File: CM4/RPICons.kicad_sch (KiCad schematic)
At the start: 2 parts, among them U1 Compute_Module_4_Connectors, U2 Compute_Module_4_Connectors

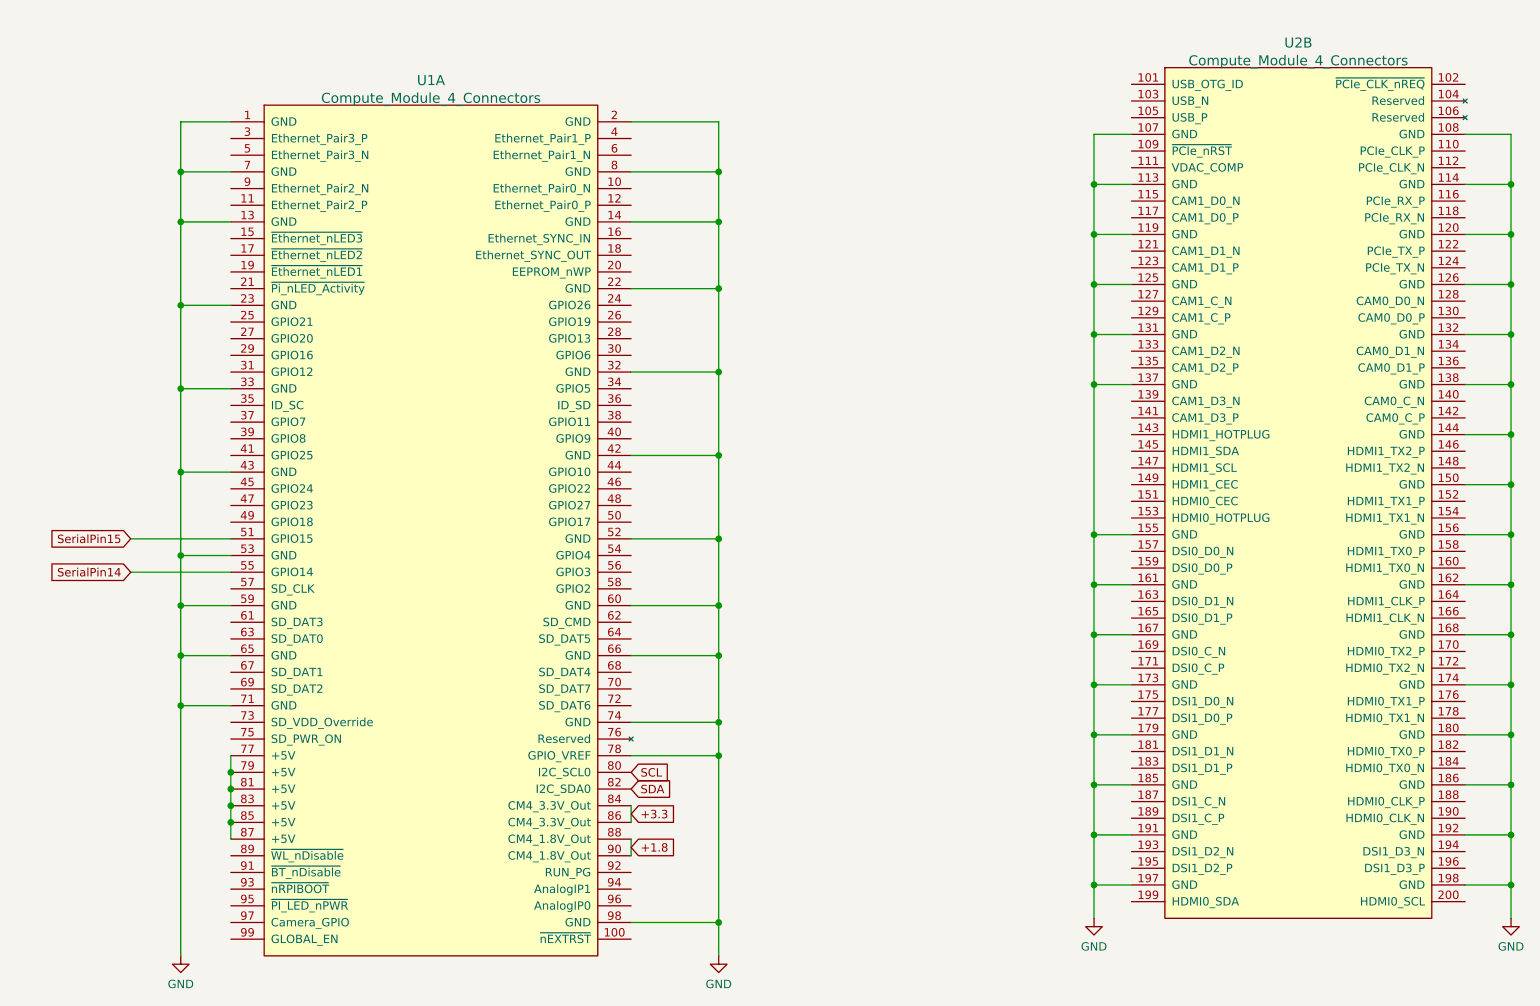
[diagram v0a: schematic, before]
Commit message: Added Power Control Relay
also cleaned up some junk and jank
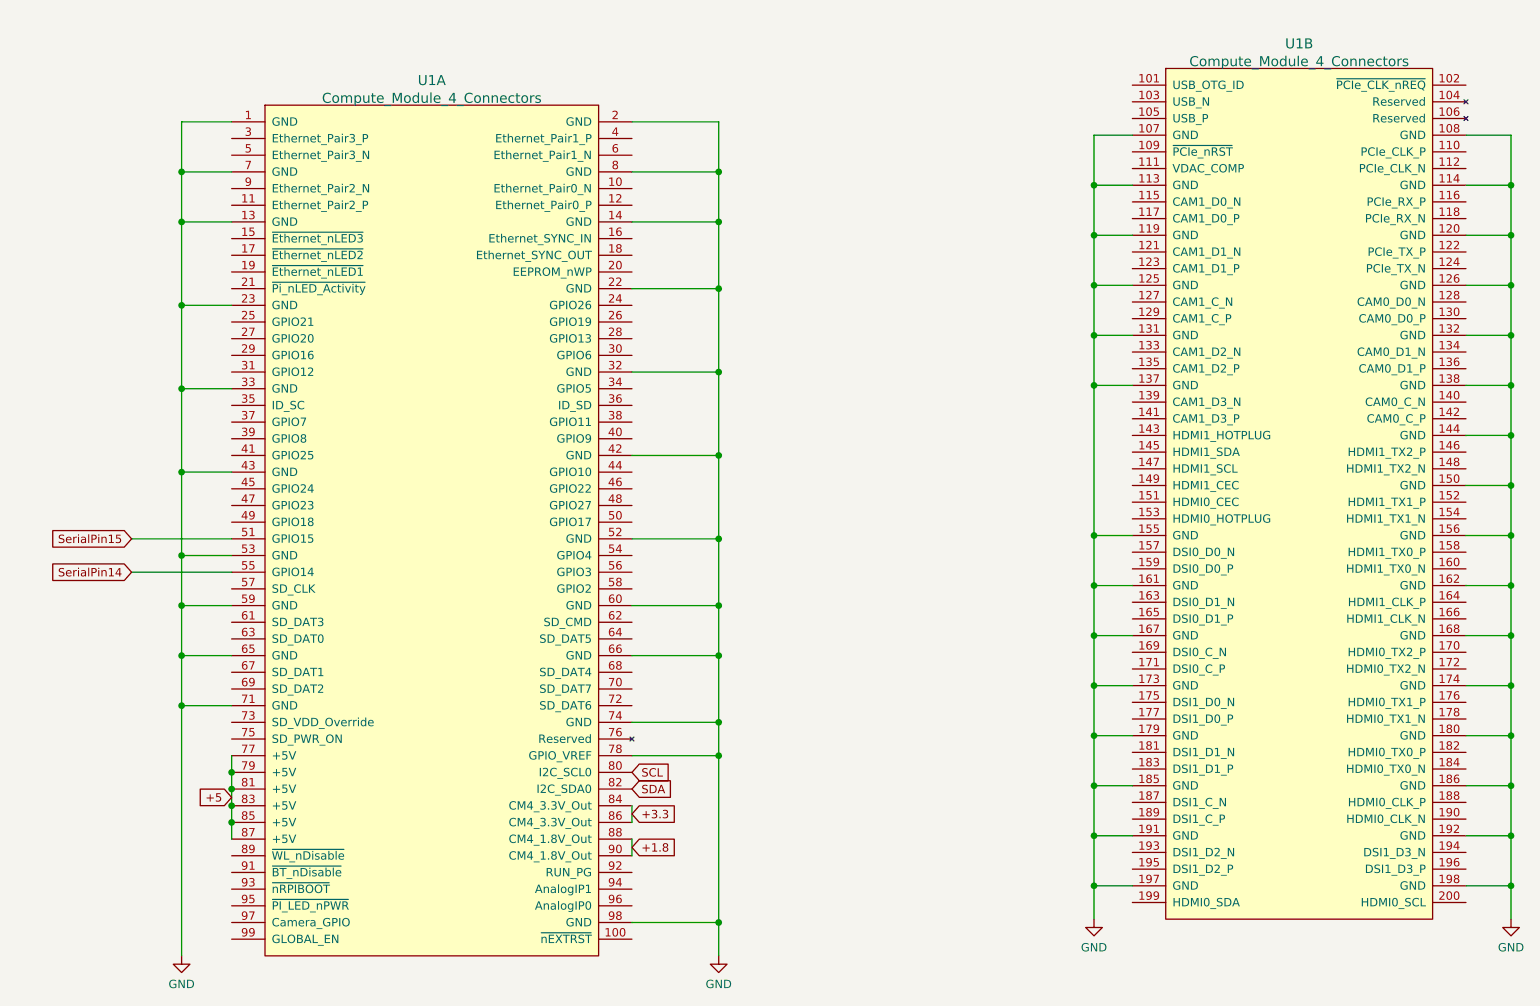
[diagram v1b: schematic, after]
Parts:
- renumbered U2 to U1
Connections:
- net +5: now reaches U1.77 (+5V), U1.79 (+5V), U1.81 (+5V), U1.83 (+5V), U1.85 (+5V), U1.87 (+5V)

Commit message: Removed Keyboard Matrix Diodes and Added PowerLED and ActivityLED
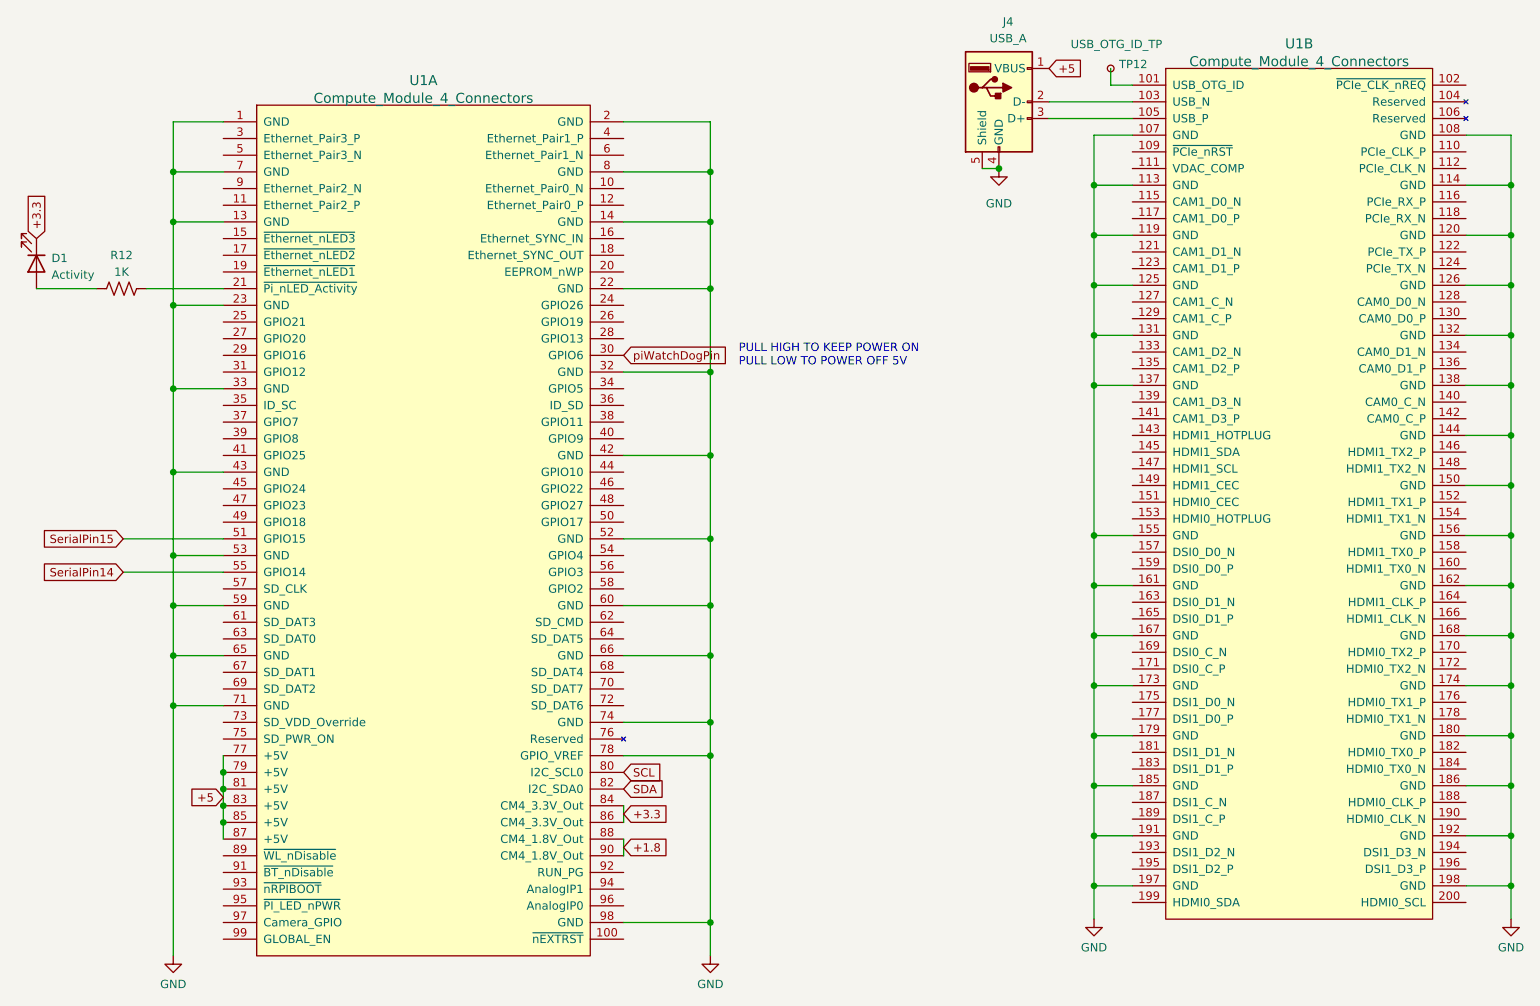
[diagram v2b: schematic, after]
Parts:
- added D1: Activity, LED_SMD:LED_2010_5025Metric, symbol Device:LED
- added J4: USB_A, Connector_USB:USB_A_Stewart_SS-52100-001_Horizontal, symbol Connector:USB_A
- added R12: 1K, symbol Device:R_US
- added TP12: USB_OTG_ID_TP, symbol Connector:TestPoint_Small
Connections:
- net +3.3: now also D1.1 (K)
- net +5: now also J4.1 (VBUS)
- net GND: now also J4.4 (GND), J4.5 (Shield)
- net at U1.101 (USB_OTG_ID): now also TP12.1
- net at U1.103 (USB_N): now also J4.2 (D-)
- net at U1.105 (USB_P): now also J4.3 (D+)
- net at U1.21 (~Pi_nLED_Activity): now also R12.2
- net piWatchDogPin: now reaches U1.30 (GPIO6)
- new net: D1.2 (A), R12.1
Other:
- note added: "PULL HIGH TO KEEP POWER ON PULL LOW TO POWER OFF 5V"
- moved on the sheet: U1A

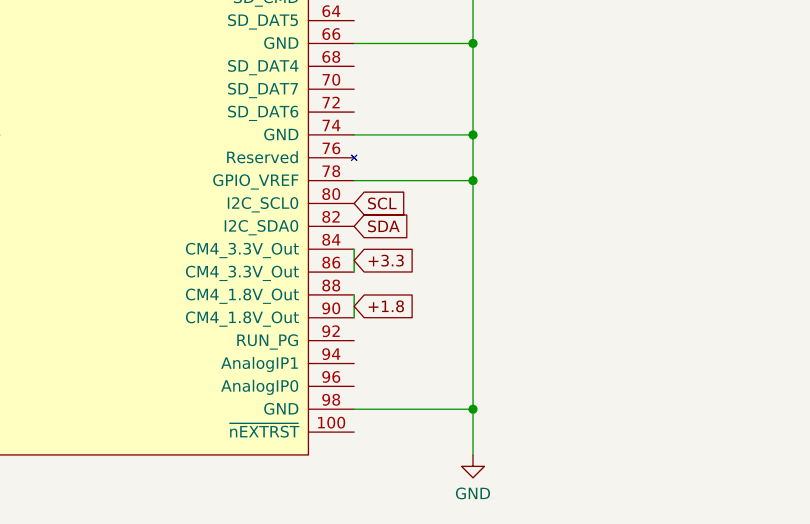
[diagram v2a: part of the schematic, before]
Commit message: Added high current 3.3v supply
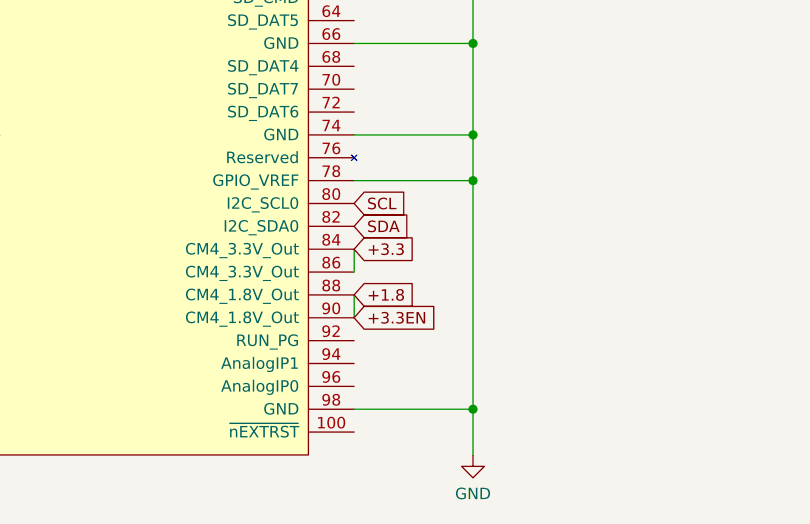
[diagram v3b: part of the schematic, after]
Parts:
- TP12: footprint (none) -> TestPoint:TestPoint_Pad_D1.0mm
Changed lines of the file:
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@@
     )
   )
-  (global_label "+3.3" (shape input) (at 112.522 138.43 0)
+  (global_label "+3.3" (shape input) (at 112.522 137.16 0)
     (effects (font (size 1.27 1.27)) (justify left))
-    (property "Intersheet References" "${INTERSHEET_REFS}" (id 0) (at 119.5313 138.3506 0)
+    (property "Intersheet References" "${INTERSHEET_REFS}" (id 0) (at 119.5313 137.0806 0)
       (effects (font (size 1.27 1.27)) (justify left) hide)
     )
   )
-  (global_label "+1.8" (shape input) (at 112.522 143.51 0)
+  (global_label "+1.8" (shape input) (at 112.522 142.24 0)
     (effects (font (size 1.27 1.27)) (justify left))
-    (property "Intersheet References" "${INTERSHEET_REFS}" (id 0) (at 119.5313 143.4306 0)
+    (property "Intersheet References" "${INTERSHEET_REFS}" (id 0) (at 119.5313 142.1606 0)
+      (effects (font (size 1.27 1.27)) (justify left) hide)
+    )
+  )
+  (global_label "+3.3EN" (shape input) (at 112.522 144.78 0)
+    (effects (font (size 1.27 1.27)) (justify left))
+    (property "Intersheet References" "${INTERSHEET_REFS}" (id 0) (at 122.0108 144.7006 0)
       (effects (font (size 1.27 1.27)) (justify left) hide)
     )
@@
       (effects (font (size 1.27 1.27)) (justify left))
     )
-    (property "Footprint" "" (id 2) (at 191.77 24.892 0)
+    (property "Footprint" "TestPoint:TestPoint_Pad_D1.0mm" (id 2) (at 191.77 24.892 0)
       (effects (font (size 1.27 1.27)) hide)
     )

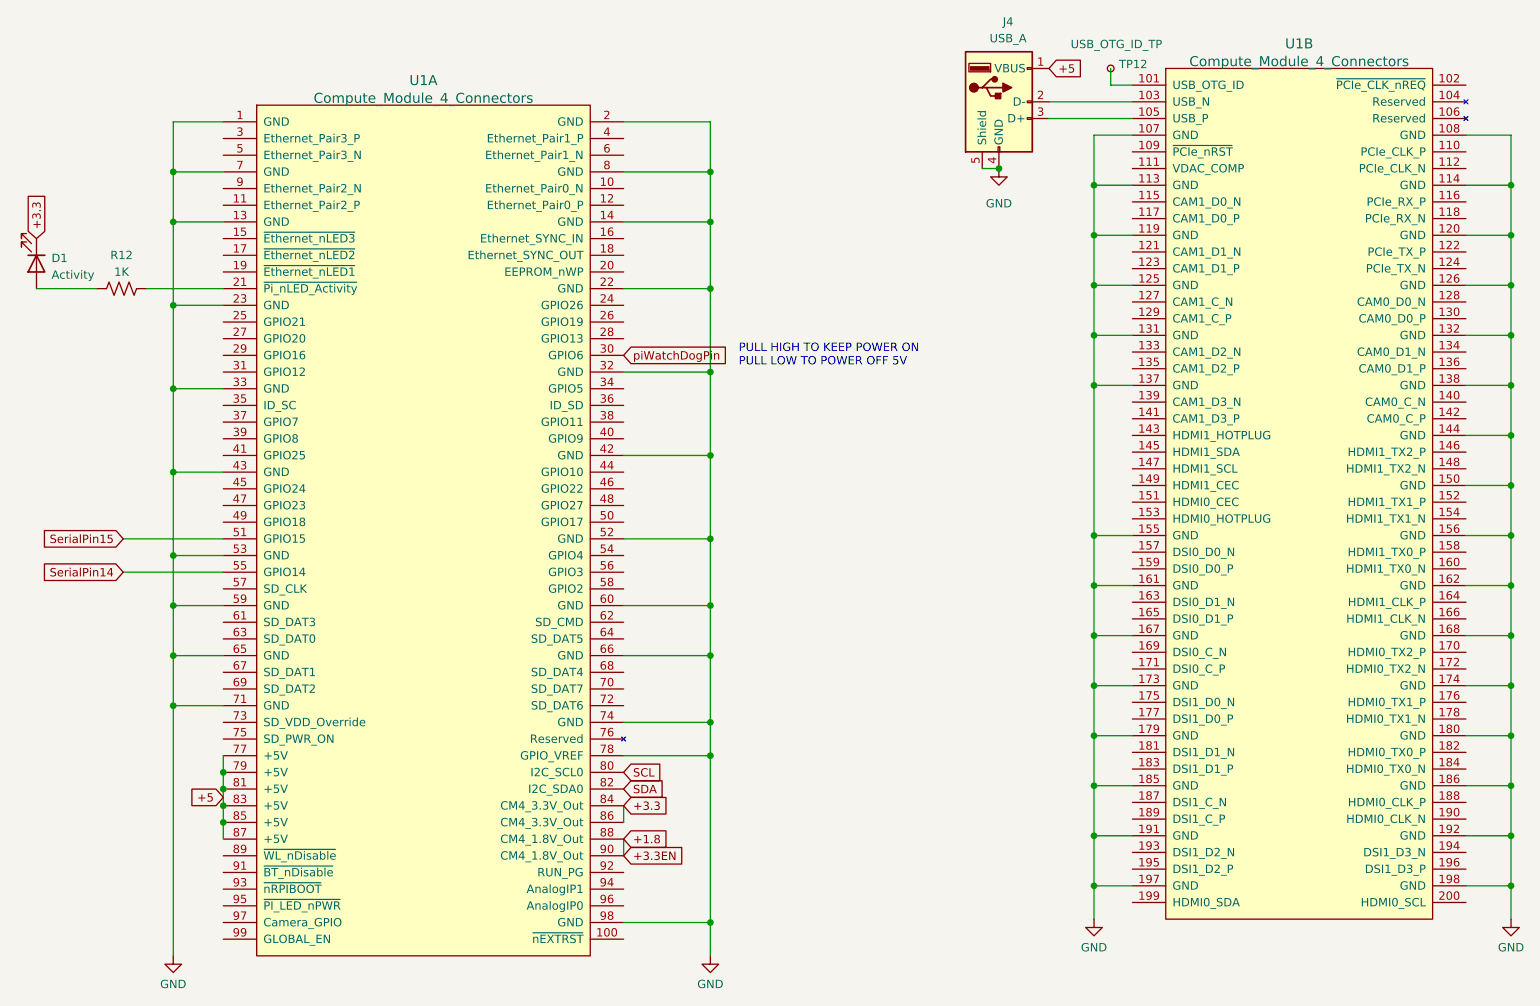
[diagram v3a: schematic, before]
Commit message: Added USB Hub Contoler and usb port internal and external
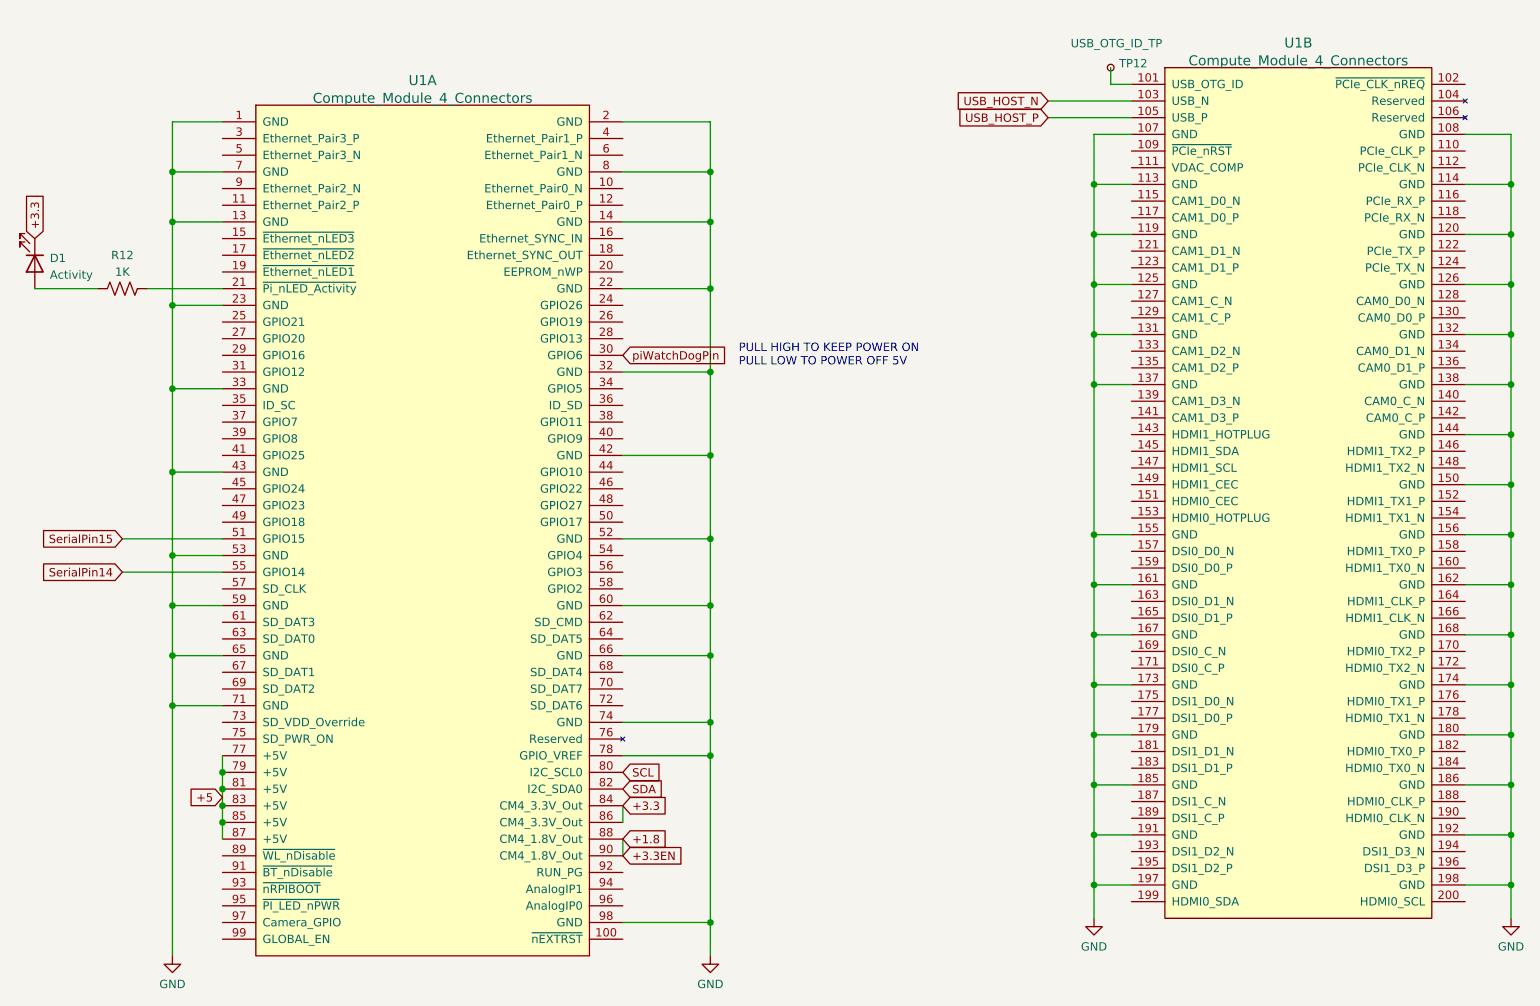
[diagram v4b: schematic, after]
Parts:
- removed J4: USB_A, Connector_USB:USB_A_Stewart_SS-52100-001_Horizontal, symbol Connector:USB_A
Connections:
- net USB_HOST_N: now reaches U1.103 (USB_N)
- net USB_HOST_P: now reaches U1.105 (USB_P)

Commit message: Added Keyboard matrix controller and indicator leds
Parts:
- D1: footprint LED_SMD:LED_2010_5025Metric -> LED_SMD:LED_1206_3216Metric_Pad1.42x1.75mm_HandSolder
- R12: footprint (none) -> Resistor_SMD:R_1206_3216Metric
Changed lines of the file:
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@@
     (property "Reference" "R12" (id 0) (at 36.195 53.34 90))
     (property "Value" "1K" (id 1) (at 36.195 55.88 90))
-    (property "Footprint" "" (id 2) (at 36.449 57.404 90)
+    (property "Footprint" "Resistor_SMD:R_1206_3216Metric" (id 2) (at 36.449 57.404 90)
       (effects (font (size 1.27 1.27)) hide)
     )
@@
       (effects (font (size 1.27 1.27)) (justify left))
     )
-    (property "Footprint" "LED_SMD:LED_2010_5025Metric" (id 2) (at 22.86 54.61 0)
+    (property "Footprint" "LED_SMD:LED_1206_3216Metric_Pad1.42x1.75mm_HandSolder" (id 2) (at 22.86 54.61 0)
       (effects (font (size 1.27 1.27)) hide)
     )
